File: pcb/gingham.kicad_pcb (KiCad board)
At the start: 2 copper layers, 285.8 x 123.8 mm, 172 parts, among them J1 Molex-0548190519, J2 ISP, J3 I2C, SW1 SW_Push, SW10 SW_Push, SW11 SW_Push, SW12 SW_Push, SW13 SW_Push, SW14 SW_Push, SW15 SW_Push, SW16 SW_Push, SW17 SW_Push, SW18 SW_Push, SW19 SW_Push, SW2 SW_Push, SW20 SW_Push, SW21 SW_Push, SW22 SW_Push, SW23 SW_Push, SW24 SW_Push, SW25 SW_Push, SW26 SW_Push, SW27 SW_Push, SW28 SW_Push, SW29 SW_Push, SW3 SW_Push, SW30 SW_Push, SW31 SW_Push, SW32 SW_Push, SW33 SW_Push, SW34 SW_Push, SW35 SW_Push, SW36 SW_Push, SW37 SW_Push, SW38 SW_Push, SW39 SW_Push, SW4 SW_Push, SW40 SW_Push, SW41 SW_Push, SW42 SW_Push, SW43 SW_Push, SW44 SW_Push, SW45 SW_Push, SW46 SW_Push, SW47 SW_Push, SW48 SW_Push, SW49 SW_Push, SW5 SW_Push, SW50 SW_Push, SW51 SW_Push, SW52 SW_Push, SW53 SW_Push, SW54 SW_Push, SW55 SW_Push, SW56 SW_Push, SW57 SW_Push, SW58 SW_Push, SW59 SW_Push, SW6 SW_Push, SW60 SW_Push, SW61 SW_Push, SW62 SW_Push, SW63 SW_Push, SW64 SW_Push, SW65 SW_Push, SW66 SW_Push, SW67 SW_Push, SW68 RESET, SW69 BOOT, SW7 SW_Push, SW70 SW_Push, SW71 SW_Push, SW8 SW_Push, SW9 SW_Push, U1 ATMEGA328-PU, U2 MCP23008-E_P, Y1 16MHz

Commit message: Gingaham
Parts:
- removed the G*** at (149.8, 159.5)
- removed tartan_pattern: G***, tartan:tartan
- added svg2mod: G***, tartan:gingham, F.Cu at (133.7, 51.3)
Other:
- board text added: "+"
- board text added: "Designed and assembled by Yiancar in Cambridge, UK Gingham V1.0 Inspired by Plaid"
- board text removed: "Designed and assembled by Yiancar in Cambridge, UK Tartar V1.0 Inspired by Plaid"
- board text removed: "Inspired by Plaid"

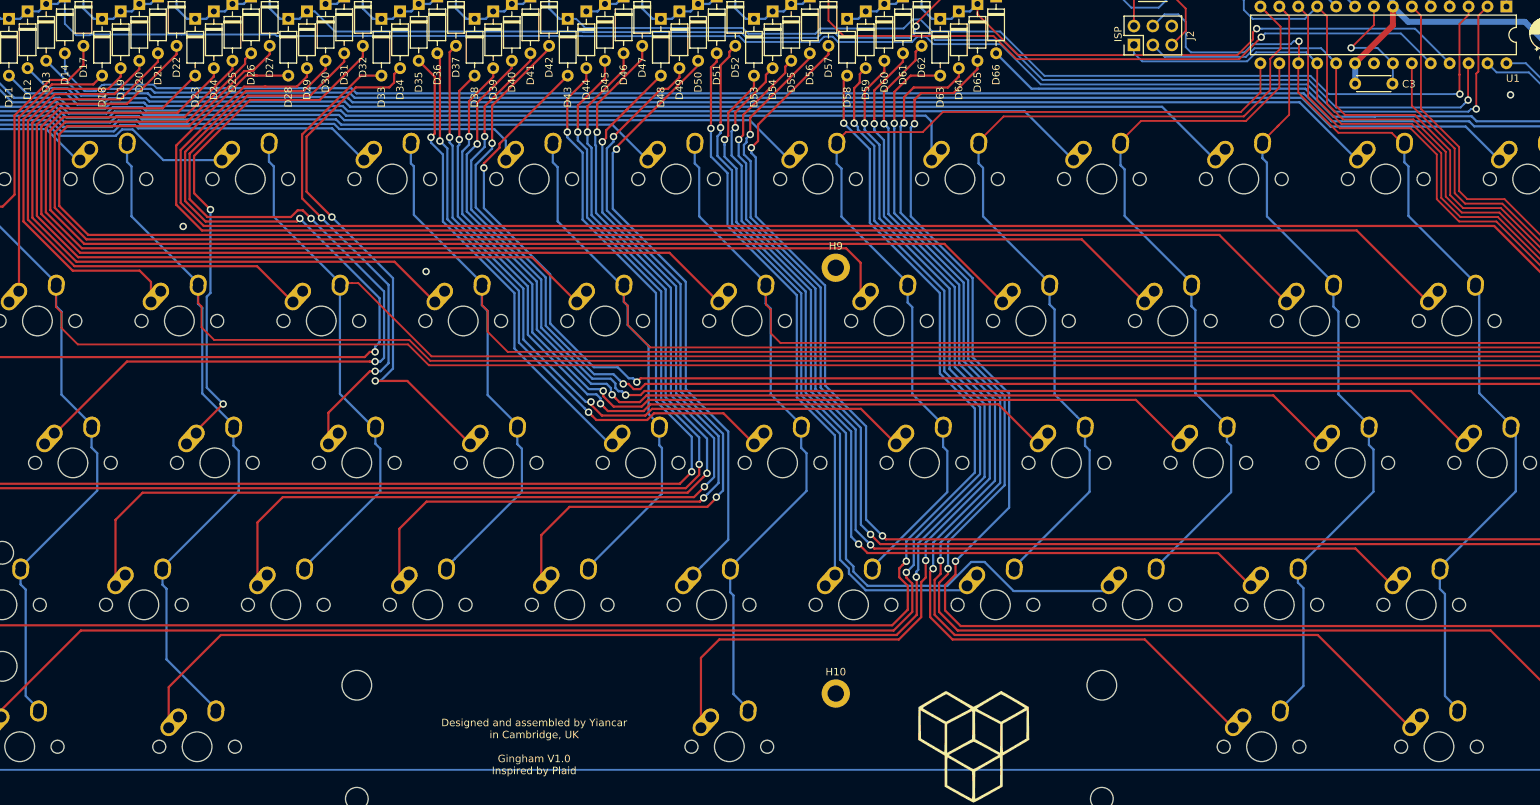
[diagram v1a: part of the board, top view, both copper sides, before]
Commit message: Relocate middle screwmounts
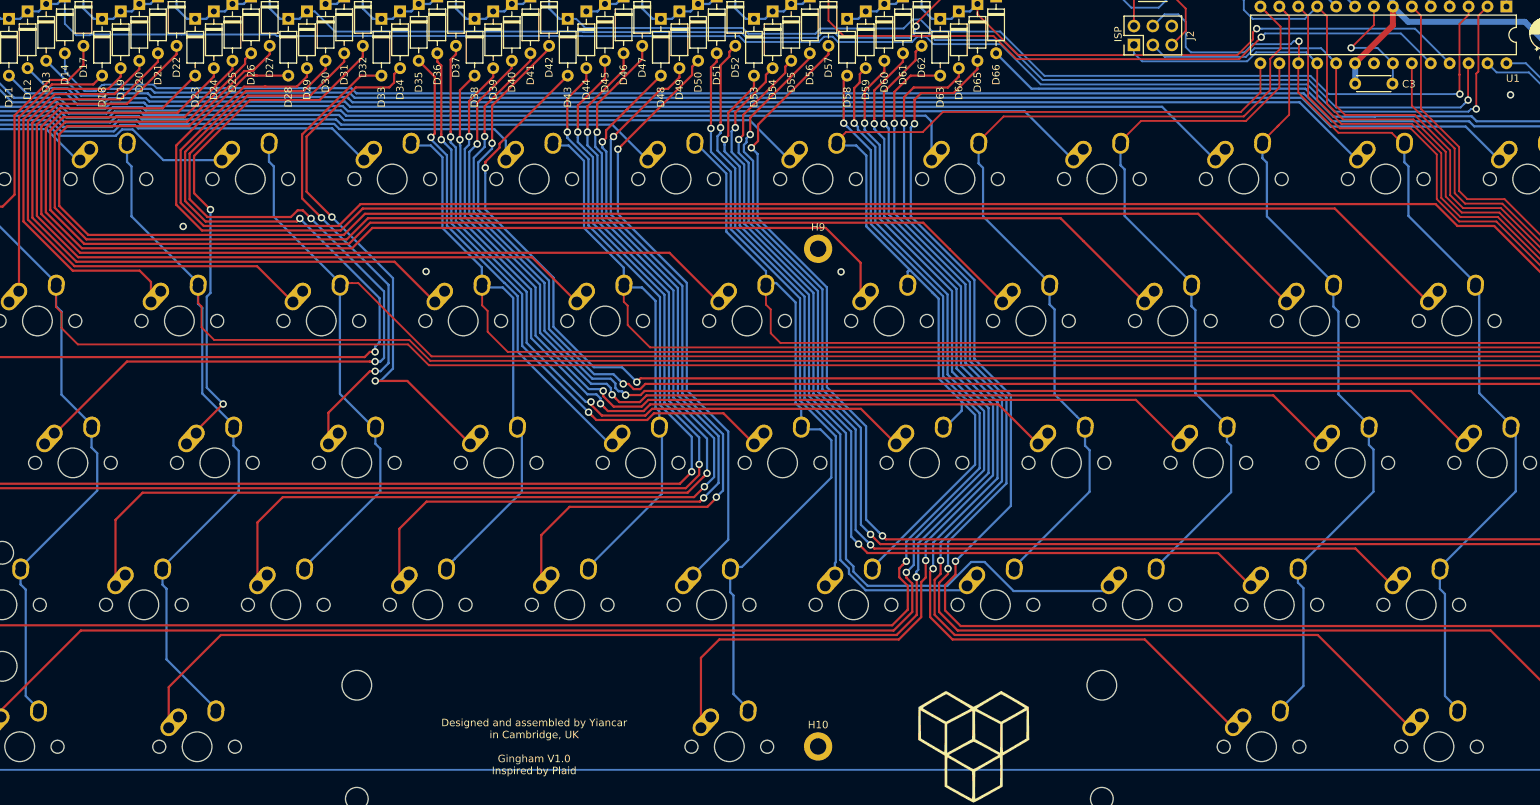
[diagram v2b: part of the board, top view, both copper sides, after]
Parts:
- moved H10 7.49 mm to (188.1, 159.5)
- moved H9 3.48 mm to (188.1, 92.7)
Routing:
- net /COL7: track 131.0 -> 143.9 mm
- net /COL6: track 288.0 -> 295.4 mm
- net /COL4: track 339.7 -> 343.5 mm
- net /COL5: track 307.9 -> 310.6 mm
- net Net-(D28-Pad2): track 200.6 -> 203.0 mm
- net Net-(D29-Pad2): track 221.4 -> 223.9 mm
- net Net-(D25-Pad2): track 172.6 -> 175.0 mm
- net Net-(D26-Pad2): track 192.7 -> 195.1 mm
- net Net-(D27-Pad2): track 213.5 -> 215.8 mm
- net Net-(D24-Pad2): track 155.3 -> 157.5 mm
- net Net-(D50-Pad2): track 82.2 -> 81.6 mm
- net Net-(D58-Pad2): track 237.5 -> 238.0 mm
- net GND: vias 5 -> 6
